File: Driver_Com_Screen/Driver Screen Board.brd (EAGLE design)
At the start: 47 x 58.1 mm, 5 parts, among them U1 XBEE_PRO_S3B

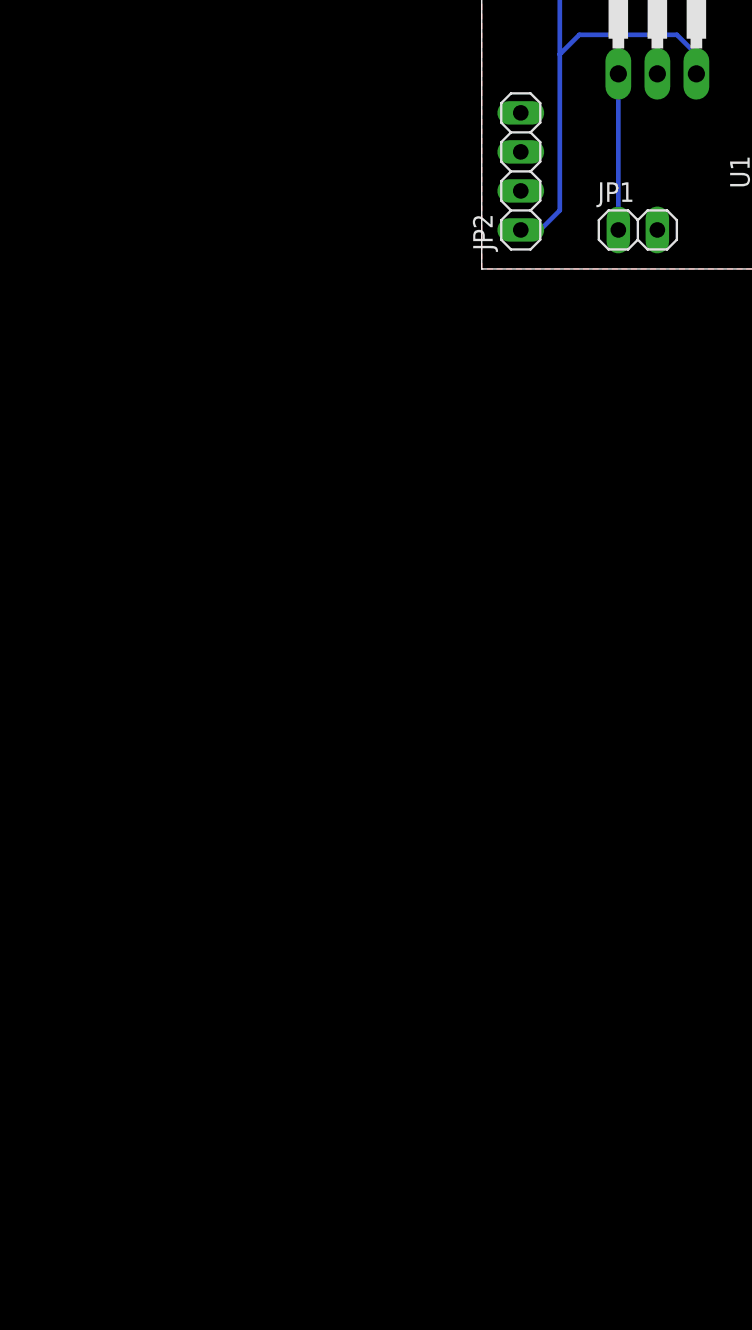
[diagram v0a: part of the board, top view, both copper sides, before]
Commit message: Updated Board to Send Messages to Driver
This board was previously used to receive messages and display on an lcd. This board will be used to send messages instead, see git issue for more info.
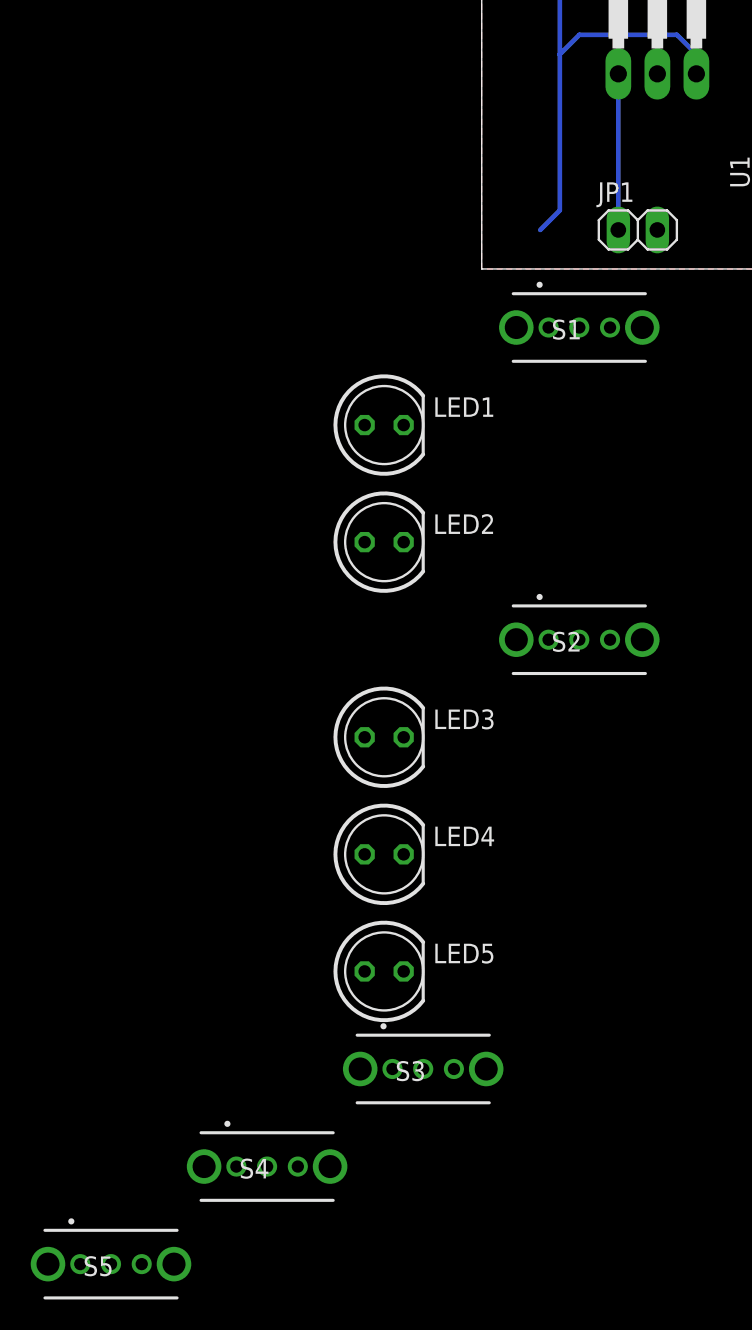
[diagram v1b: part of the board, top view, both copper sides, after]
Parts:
- removed JP2: (no value), GTOR - Connectors:1X04
- added LED1, LED2, LED3, LED4, LED5: (no value), GTOR - Passive Components:LED-5MM
- added S1, S2, S3, S4, S5: SWITCH_SLIDE_OS102011MS2QN1, GTOR - Active Components:OS102011MA1QN1
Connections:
- removed net SCL: JP2.3
- removed net SDA: JP2.2
- new net +3V3: S1.1, S2.1, S3.1, S4.1, S5.1
- new net A0: LED1.K, S1.2, U$1.14/A0
- new net A1: LED2.K, S2.2, U$1.15/A1
- new net A2: LED3.K, S3.2, U$1.16/A2
- new net A3: LED4.K, S4.2, U$1.17/A3
- new net A4: LED5.K, S5.2, U$1.18/A4/SDA
- net +5V: no longer JP2.1
- net GND: now also LED1.A, LED2.A, LED3.A, LED4.A, LED5.A, S1.3, S2.3, S3.3, S4.3, S5.3; no longer JP2.4
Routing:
- net +5V: track 66.4 -> 65.2 mm

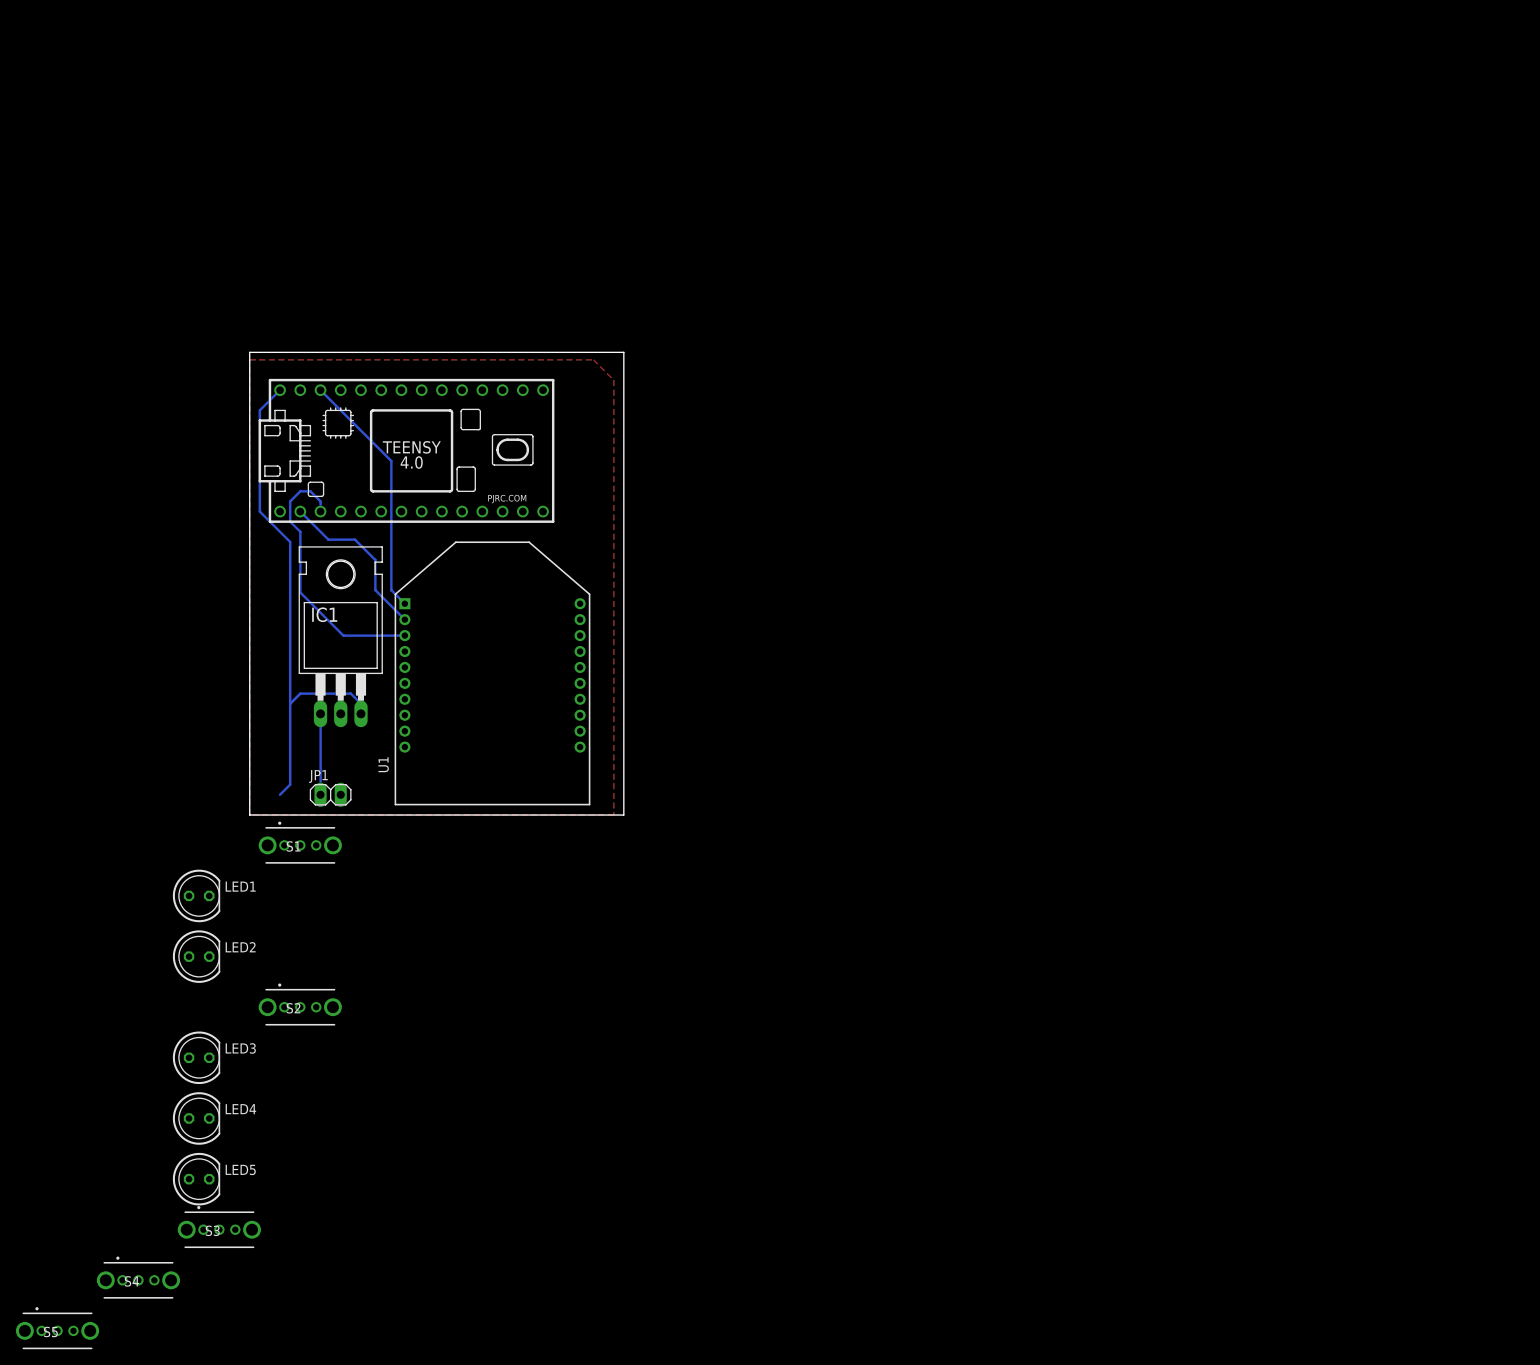
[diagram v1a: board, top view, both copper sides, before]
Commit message: Updated Board Used to Send Driver Messages
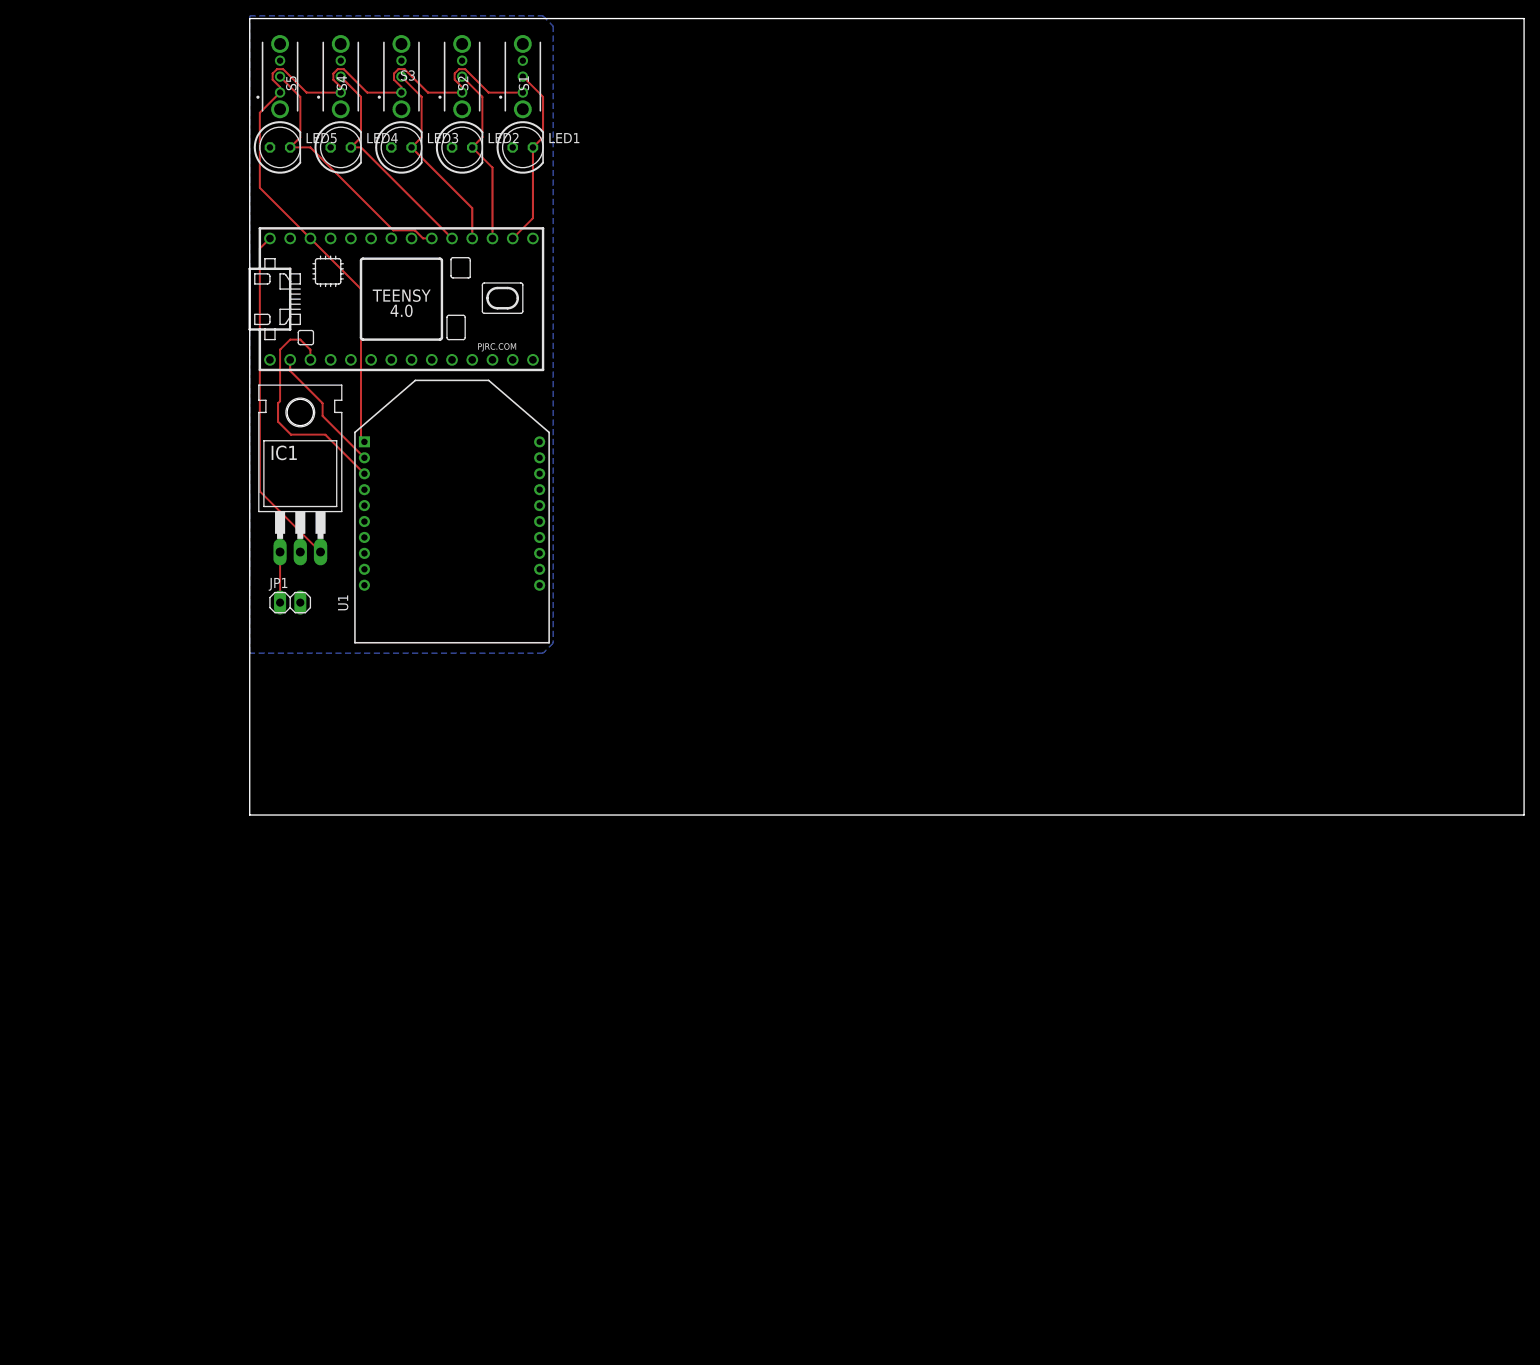
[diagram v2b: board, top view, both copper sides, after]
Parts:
- moved S5 159.9 mm to (3.81, 92.7), turned to 90 degrees
- moved S4 153.2 mm to (11.4, 92.7), turned to 90 degrees
- moved S3 146.6 mm to (19.1, 92.7), turned to 90 degrees
- moved LED5 129.9 mm to (3.81, 83.8)
- moved LED4 123.2 mm to (11.4, 83.8)
- moved S2 118.6 mm to (26.7, 92.7), turned to 90 degrees
- moved LED3 117.1 mm to (19.1, 83.8)
- moved LED2 106.8 mm to (26.7, 83.8)
- moved LED1 102.4 mm to (34.3, 83.8)
- moved S1 100.5 mm to (34.3, 92.7), turned to 90 degrees
- moved JP1 24.7 mm to (5.08, 26.7)
- moved U1 20.9 mm to (25.4, 38.1)
- moved IC1 20.9 mm to (6.35, 39.4)
- moved U$1 19.1 mm to (19.1, 64.8)
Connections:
- removed net +3V3: S1.1, S2.1, S3.1, S4.1, S5.1
- net 3V_TEENSY: now also S1.1, S2.1, S3.1, S4.1, S5.1
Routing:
- net 3V_TEENSY: track 31.2 -> 103.0 mm
- net A4: track 0.00 -> 33.0 mm
- net A3: track 0.00 -> 27.9 mm
- net A2: track 0.00 -> 25.1 mm
- net A1: track 0.00 -> 23.0 mm
- net A0: track 0.00 -> 23.0 mm
- net +5V: track 65.2 -> 43.1 mm
- net XBEE_TX: track 21.0 -> 16.2 mm
- net XBEE_RX: track 33.5 -> 28.8 mm
- net VCC: track 10.2 -> 6.35 mm
- added copper zone on layer 16, net GND
- removed copper zone on layer 1, net GND
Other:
- board size 47 x 58.1 mm -> 160 x 100 mm
